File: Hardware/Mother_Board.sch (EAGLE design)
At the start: 11 parts, among them IC1 MAX3232CPE, U1 PIC18F26K22-I/SP

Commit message: Added LCD display module and SPI EEPROM to the schematics.
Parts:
- added JP3: (no value), pinhead:PINHD-1X8
- added JP4, JP5: (no value), pinhead:PINHD-1X6
- added R3: 22R 0.5W, resistor:R-EU_0207/10
- added R4: 10K, rcl:POTENTIOMETER_PT-10S
- added U2: 25LC1024-E/SM, 25LC1024:25LC1024-E/SM
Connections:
- new net N$11: JP3.8, U1.RA0
- new net N$12: JP3.7, U1.RA1
- new net N$15: JP3.6, U1.RA2
- new net N$16: JP3.5, U1.RA3
- new net N$17: JP3.4, U1.RA4
- new net N$18: JP3.3, U1.RA5
- new net N$19: JP3.2, U1.RA6
- new net N$20: JP3.1, U1.RA7
- new net N$21: U1.RC4, U2.SI
- new net N$22: U1.RC3, U2.SCK
- new net N$23: U1.RC5, U2.SO
- new net N$24: U1.RC2, U2.CS*
- new net N$25: JP5.3, R4.1
- new net N$26: JP4.1, U1.RB5
- new net N$27: JP4.2, U1.RB4
- new net N$28: JP4.3, U1.RB3
- new net N$29: JP4.4, U1.RB2
- new net N$30: JP4.5, U1.RB1
- new net N$31: JP4.6, U1.RB0
- new net N$32: JP5.2, R4.3
- new net N$33: JP5.6, R3.2
- net GND: now also JP5.4, JP5.5, U2.VSS
- net VCC: now also JP5.1, R3.1, R4.2, U2.HOLD*, U2.VCC, U2.WP*
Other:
- note added: "/CS1"
- note added: "/CS2"
- note added: "A"
- note added: "D/I"
- note added: "DB0"
- note added: "DB1"
- note added: "DB2"
- note added: "DB3"
- note added: "DB4"
- note added: "DB5"
- note added: "DB6"
- note added: "DB7"
- note added: "Display control"
- note added: "Display data"
- note added: "Display power"
- note added: "E"
- note added: "K"
- note added: "Keyboard"
- note added: "R/W"
- note added: "RST"
- note added: "UART"
- note added: "Vcc"
- note added: "Vee"
- note added: "Vo"
- note added: "Vss"
- note removed: "To DIN keyboard connector"
- note removed: "To Sub-D 9 connector"
- moved on the sheet: C1, C2, C3, C4, C5, IC1, IC1P, JP1

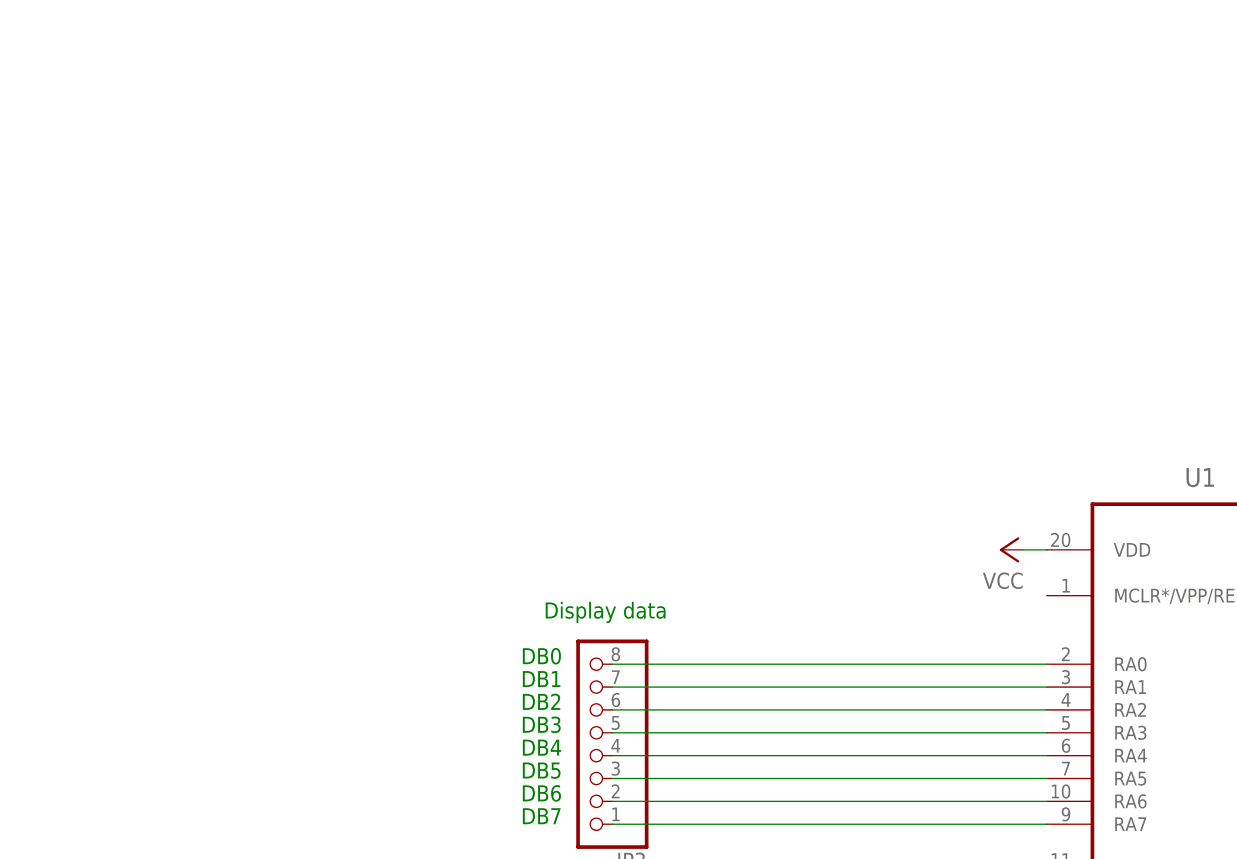
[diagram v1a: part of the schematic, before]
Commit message: Added led and power supply to the schematics.
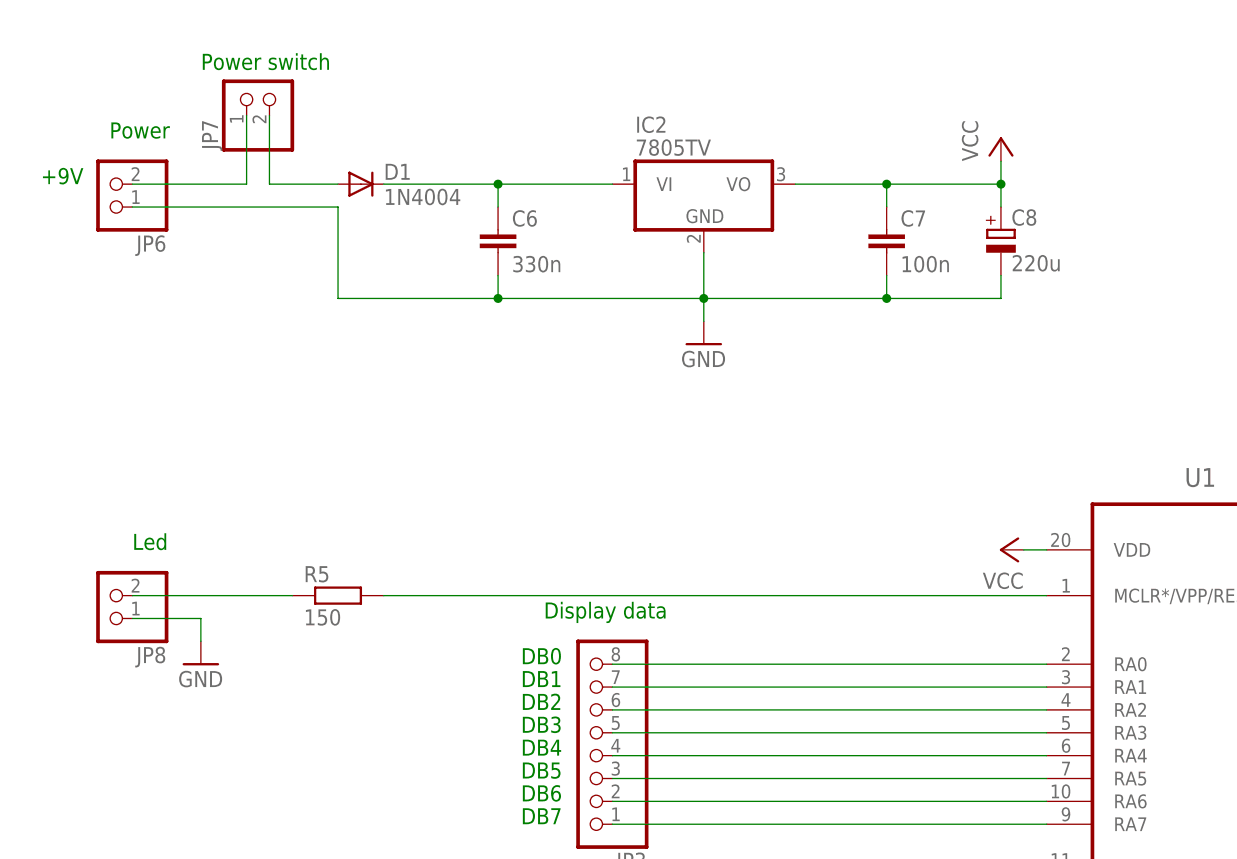
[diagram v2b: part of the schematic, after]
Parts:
- added C6: 330n, rcl:C-EU025-050X050
- added C7: 100n, rcl:C-EU025-030X050
- added C8: 220u, rcl:CPOL-EUB45181A
- added D1: 1N4004, diode:1N4004
- added IC2: 7805TV, linear:7805TV
- added JP6, JP7, JP8: (no value), pinhead:PINHD-1X2
- added R5: 150, rcl:R-EU_0207/10
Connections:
- new net N$34: JP6.2, JP7.1
- new net N$35: D1.A, JP7.2
- new net N$36: C6.1, D1.C, IC2.VI
- new net N$37: R5.2, U1.MCLR*/VPP/RE3
- new net N$38: JP8.2, R5.1
- net GND: now also C6.2, C7.2, C8.-, IC2.GND, JP6.1, JP8.1
- net VCC: now also C7.1, C8.+, IC2.VO
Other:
- note added: "+9V"
- note added: "Led"
- note added: "Power"
- note added: "Power switch"
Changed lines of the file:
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@@
 <part name="R3" library="resistor" deviceset="R-EU_" device="0207/10" value="22R 0.5W"/>
 <part name="P+7" library="supply1" deviceset="VCC" device=""/>
+<part name="IC2" library="linear" deviceset="78*" device="TV" technology="05"/>
+<part name="C6" library="rcl" deviceset="C-EU" device="025-050X050" value="330n"/>
+<part name="D1" library="diode" deviceset="1N4004" device=""/>
+<part name="C8" library="rcl" deviceset="CPOL-EU" device="B45181A" value="220u"/>
+<part name="JP6" library="pinhead" deviceset="PINHD-1X2" device=""/>
+<part name="GND8" library="supply1" deviceset="GND" device=""/>
+<part name="P+9" library="supply1" deviceset="VCC" device=""/>
+<part name="JP7" library="pinhead" deviceset="PINHD-1X2" device=""/>
+<part name="JP8" library="pinhead" deviceset="PINHD-1X2" device=""/>
+<part name="R5" library="rcl" deviceset="R-EU_" device="0207/10" value="150"/>
+<part name="GND10" library="supply1" deviceset="GND" device=""/>
+<part name="C7" library="rcl" deviceset="C-EU" device="025-030X050" value="100n"/>
 </parts>
 <sheets>
@@
 <text x="142.24" y="30.48" size="1.778" layer="91">R/W</text>
 <text x="142.24" y="27.94" size="1.778" layer="91">RST</text>
+<text x="-73.66" y="114.3" size="1.778" layer="91">+9V</text>
+<text x="-66.04" y="119.38" size="1.778" layer="91">Power</text>
+<text x="-55.88" y="127" size="1.778" layer="91">Power switch</text>
+<text x="-63.5" y="73.66" size="1.778" layer="91">Led</text>
 </plain>
 <instances>
@@
 <instance part="R3" gate="G$1" x="129.54" y="-20.32" rot="R90"/>
 <instance part="P+7" gate="VCC" x="129.54" y="-30.48" rot="R180"/>
+<instance part="IC2" gate="A1" x="0" y="114.3"/>
+<instance part="C6" gate="G$1" x="-22.86" y="109.22"/>
+<instance part="D1" gate="1" x="-38.1" y="114.3"/>
+<instance part="C8" gate="G$1" x="33.02" y="109.22"/>
+<instance part="JP6" gate="G$1" x="-66.04" y="114.3" rot="R180"/>
+<instance part="GND8" gate="1" x="0" y="96.52"/>
+<instance part="P+9" gate="VCC" x="33.02" y="119.38"/>
+<instance part="JP7" gate="G$1" x="-48.26" y="124.46" rot="R90"/>
+<instance part="JP8" gate="G$1" x="-66.04" y="68.58" rot="R180"/>
+<instance part="R5" gate="G$1" x="-40.64" y="68.58"/>
+<instance part="GND10" gate="1" x="-55.88" y="60.96"/>
+<instance part="C7" gate="G$1" x="20.32" y="109.22"/>
 </instances>
 <busses>
@@
 <wire x1="129.54" y1="-5.08" x2="116.84" y2="-5.08" width="0.1524" layer="91"/>
 <junction x="129.54" y="-5.08"/>
+</segment>
+<segment>
+<pinref part="JP6" gate="G$1" pin="1"/>
+<wire x1="-63.5" y1="111.76" x2="-40.64" y2="111.76" width="0.1524" layer="91"/>
+<wire x1="-40.64" y1="111.76" x2="-40.64" y2="101.6" width="0.1524" layer="91"/>
+<wire x1="-40.64" y1="101.6" x2="-22.86" y2="101.6" width="0.1524" layer="91"/>
+<pinref part="C6" gate="G$1" pin="2"/>
+<wire x1="0" y1="101.6" x2="20.32" y2="101.6" width="0.1524" layer="91"/>
+<wire x1="20.32" y1="101.6" x2="33.02" y2="101.6" width="0.1524" layer="91"/>
+<wire x1="-22.86" y1="104.14" x2="-22.86" y2="101.6" width="0.1524" layer="91"/>
+<pinref part="GND8" gate="1" pin="GND"/>
+<wire x1="-22.86" y1="101.6" x2="0" y2="101.6" width="0.1524" layer="91"/>
+<wire x1="0" y1="99.06" x2="0" y2="101.6" width="0.1524" layer="91"/>
+<pinref part="IC2" gate="A1" pin="GND"/>
+<wire x1="0" y1="101.6" x2="0" y2="106.68" width="0.1524" layer="91"/>
+<wire x1="20.32" y1="101.6" x2="20.32" y2="104.14" width="0.1524" layer="91"/>
+<pinref part="C8" gate="G$1" pin="-"/>
+<wire x1="33.02" y1="101.6" x2="33.02" y2="104.14" width="0.1524" layer="91"/>
+<junction x="-22.86" y="101.6"/>
+<junction x="0" y="101.6"/>
+<junction x="20.32" y="101.6"/>
+<pinref part="C7" gate="G$1" pin="2"/>
+</segment>
+<segment>
+<pinref part="JP8" gate="G$1" pin="1"/>
+<wire x1="-63.5" y1="66.04" x2="-55.88" y2="66.04" width="0.1524" layer="91"/>
+<pinref part="GND10" gate="1" pin="GND"/>
+<wire x1="-55.88" y1="66.04" x2="-55.88" y2="63.5" width="0.1524" layer="91"/>
 </segment>
 </net>
@@
 <wire x1="129.54" y1="-25.4" x2="129.54" y2="-27.94" width="0.1524" layer="91"/>
 </segment>
+<segment>
+<pinref part="IC2" gate="A1" pin="VO"/>
+<wire x1="10.16" y1="114.3" x2="20.32" y2="114.3" width="0.1524" layer="91"/>
+<wire x1="20.32" y1="111.76" x2="20.32" y2="114.3" width="0.1524" layer="91"/>
+<wire x1="20.32" y1="114.3" x2="33.02" y2="114.3" width="0.1524" layer="91"/>
+<pinref part="C8" gate="G$1" pin="+"/>
+<wire x1="33.02" y1="114.3" x2="33.02" y2="111.76" width="0.1524" layer="91"/>
+<junction x="20.32" y="114.3"/>
+<pinref part="P+9" gate="VCC" pin="VCC"/>
+<wire x1="33.02" y1="116.84" x2="33.02" y2="114.3" width="0.1524" layer="91"/>
+<junction x="33.02" y="114.3"/>
+<pinref part="C7" gate="G$1" pin="1"/>
+</segment>
 </net>
 <net name="N$6" class="0">
@@
 </segment>
 </net>
+<net name="N$36" class="0">
+<segment>
+<pinref part="D1" gate="1" pin="C"/>
+<pinref part="IC2" gate="A1" pin="VI"/>
+<wire x1="-35.56" y1="114.3" x2="-22.86" y2="114.3" width="0.1524" layer="91"/>
+<pinref part="C6" gate="G$1" pin="1"/>
+<wire x1="-22.86" y1="114.3" x2="-10.16" y2="114.3" width="0.1524" layer="91"/>
+<wire x1="-22.86" y1="114.3" x2="-22.86" y2="111.76" width="0.1524" layer="91"/>
+<junction x="-22.86" y="114.3"/>
+</segment>
+</net>
+<net name="N$34" class="0">
+<segment>
+<pinref part="JP6" gate="G$1" pin="2"/>
+<wire x1="-63.5" y1="114.3" x2="-50.8" y2="114.3" width="0.1524" layer="91"/>
+<pinref part="JP7" gate="G$1" pin="1"/>
+<wire x1="-50.8" y1="114.3" x2="-50.8" y2="121.92" width="0.1524" layer="91"/>
+</segment>
+</net>
+<net name="N$35" class="0">
+<segment>
+<pinref part="JP7" gate="G$1" pin="2"/>
+<wire x1="-48.26" y1="121.92" x2="-48.26" y2="114.3" width="0.1524" layer="91"/>
+<pinref part="D1" gate="1" pin="A"/>
+<wire x1="-48.26" y1="114.3" x2="-40.64" y2="114.3" width="0.1524" layer="91"/>
+</segment>
+</net>
+<net name="N$37" class="0">
+<segment>
+<pinref part="U1" gate="A" pin="MCLR*/VPP/RE3"/>
+<wire x1="38.1" y1="68.58" x2="-35.56" y2="68.58" width="0.1524" layer="91"/>
+<pinref part="R5" gate="G$1" pin="2"/>
+</segment>
+</net>
+<net name="N$38" class="0">
+<segment>
+<pinref part="JP8" gate="G$1" pin="2"/>
+<pinref part="R5" gate="G$1" pin="1"/>
+<wire x1="-63.5" y1="68.58" x2="-45.72" y2="68.58" width="0.1524" layer="91"/>
+</segment>
+</net>

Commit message: Added routed PCB.
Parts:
- JP1: value (none) -> UART
- JP2: value (none) -> Keyboard
- JP3: value (none) -> Display data
- JP4: value (none) -> Display control
- JP5: value (none) -> Display power
- JP6: value (none) -> Power
- JP7: value (none) -> Power switch
- JP8: value (none) -> Led
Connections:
- net N$19: now also U1.RA7; no longer U1.RA6
- net N$20: now also U1.RA6; no longer U1.RA7
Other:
- note added: "Routing optimization"
- note removed: "Display control"
- note removed: "Display data"
- note removed: "Display power"
- note removed: "Keyboard"
- note removed: "Led"
- note removed: "Power"
- note removed: "Power switch"
- note removed: "UART"
- moved on the sheet: C5, IC1P
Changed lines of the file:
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@@
 <part name="GND3" library="supply1" deviceset="GND" device=""/>
 <part name="P+1" library="supply1" deviceset="VCC" device=""/>
-<part name="JP1" library="pinhead" deviceset="PINHD-1X3" device=""/>
+<part name="JP1" library="pinhead" deviceset="PINHD-1X3" device="" value="UART"/>
 <part name="GND4" library="supply1" deviceset="GND" device=""/>
-<part name="JP2" library="pinhead" deviceset="PINHD-1X4" device=""/>
+<part name="JP2" library="pinhead" deviceset="PINHD-1X4" device="" value="Keyboard"/>
 <part name="P+2" library="supply1" deviceset="VCC" device=""/>
 <part name="GND5" library="supply1" deviceset="GND" device=""/>
@@
 <part name="R2" library="rcl" deviceset="R-EU_" device="0207/10" value="1K"/>
 <part name="P+4" library="supply1" deviceset="VCC" device=""/>
-<part name="JP3" library="pinhead" deviceset="PINHD-1X8" device=""/>
+<part name="JP3" library="pinhead" deviceset="PINHD-1X8" device="" value="Display data"/>
 <part name="U2" library="25LC1024" deviceset="25LC1024-E/SM" device=""/>
 <part name="GND7" library="supply1" deviceset="GND" device=""/>
 <part name="P+5" library="supply1" deviceset="VCC" device=""/>
 <part name="P+6" library="supply1" deviceset="VCC" device=""/>
-<part name="JP4" library="pinhead" deviceset="PINHD-1X6" device=""/>
-<part name="JP5" library="pinhead" deviceset="PINHD-1X6" device=""/>
+<part name="JP4" library="pinhead" deviceset="PINHD-1X6" device="" value="Display control"/>
+<part name="JP5" library="pinhead" deviceset="PINHD-1X6" device="" value="Display power"/>
 <part name="R4" library="rcl" deviceset="POTENTIOMETER_" device="PT-10S" value="10K"/>
 <part name="P+8" library="supply1" deviceset="VCC" device=""/>
@@
 <part name="D1" library="diode" deviceset="1N4004" device=""/>
 <part name="C8" library="rcl" deviceset="CPOL-EU" device="B45181A" value="220u"/>
-<part name="JP6" library="pinhead" deviceset="PINHD-1X2" device=""/>
+<part name="JP6" library="pinhead" deviceset="PINHD-1X2" device="" value="Power"/>
 <part name="GND8" library="supply1" deviceset="GND" device=""/>
 <part name="P+9" library="supply1" deviceset="VCC" device=""/>
-<part name="JP7" library="pinhead" deviceset="PINHD-1X2" device=""/>
-<part name="JP8" library="pinhead" deviceset="PINHD-1X2" device=""/>
+<part name="JP7" library="pinhead" deviceset="PINHD-1X2" device="" value="Power switch"/>
+<part name="JP8" library="pinhead" deviceset="PINHD-1X2" device="" value="Led"/>
 <part name="R5" library="rcl" deviceset="R-EU_" device="0207/10" value="150"/>
 <part name="GND10" library="supply1" deviceset="GND" device=""/>
@@
 <sheet>
 <plain>
-<text x="172.72" y="63.5" size="1.778" layer="91">UART</text>
-<text x="17.78" y="-25.4" size="1.778" layer="91">Keyboard</text>
-<text x="-17.78" y="66.04" size="1.778" layer="91">Display data</text>
 <text x="-20.32" y="60.96" size="1.778" layer="91">DB0</text>
 <text x="-20.32" y="58.42" size="1.778" layer="91">DB1</text>
@@
 <text x="-20.32" y="50.8" size="1.778" layer="91">DB4</text>
 <text x="-20.32" y="48.26" size="1.778" layer="91">DB5</text>
-<text x="-20.32" y="45.72" size="1.778" layer="91">DB6</text>
-<text x="-20.32" y="43.18" size="1.778" layer="91">DB7</text>
-<text x="129.54" y="48.26" size="1.778" layer="91">Display control</text>
+<text x="-20.32" y="43.18" size="1.778" layer="91">DB6</text>
+<text x="-20.32" y="45.72" size="1.778" layer="91">DB7</text>
 <text x="142.24" y="5.08" size="1.778" layer="91">Vcc</text>
 <text x="142.24" y="2.54" size="1.778" layer="91">Vo</text>
@@
 <text x="142.24" y="-5.08" size="1.778" layer="91">K</text>
 <text x="142.24" y="-7.62" size="1.778" layer="91">A</text>
-<text x="129.54" y="12.7" size="1.778" layer="91">Display power</text>
 <text x="142.24" y="40.64" size="1.778" layer="91">/CS1</text>
 <text x="142.24" y="38.1" size="1.778" layer="91">/CS2</text>
@@
 <text x="142.24" y="27.94" size="1.778" layer="91">RST</text>
 <text x="-73.66" y="114.3" size="1.778" layer="91">+9V</text>
-<text x="-66.04" y="119.38" size="1.778" layer="91">Power</text>
-<text x="-55.88" y="127" size="1.778" layer="91">Power switch</text>
-<text x="-63.5" y="73.66" size="1.778" layer="91">Led</text>
+<text x="5.08" y="38.1" size="1.778" layer="91">Routing optimization</text>
 </plain>
 <instances>
@@
 <instance part="GND1" gate="1" x="167.64" y="83.82"/>
 <instance part="GND2" gate="1" x="167.64" y="96.52"/>
-<instance part="IC1" gate="P" x="139.7" y="116.84"/>
-<instance part="C5" gate="G$1" x="127" y="119.38"/>
-<instance part="GND3" gate="1" x="139.7" y="104.14"/>
-<instance part="P+1" gate="VCC" x="139.7" y="129.54"/>
+<instance part="IC1" gate="P" x="139.7" y="127"/>
+<instance part="C5" gate="G$1" x="127" y="129.54"/>
+<instance part="GND3" gate="1" x="139.7" y="111.76"/>
+<instance part="P+1" gate="VCC" x="139.7" y="142.24"/>
 <instance part="JP1" gate="A" x="177.8" y="71.12"/>
 <instance part="GND4" gate="1" x="170.18" y="60.96"/>
@@
 <pinref part="IC1" gate="P" pin="GND"/>
 <pinref part="GND3" gate="1" pin="GND"/>
-<wire x1="139.7" y1="106.68" x2="139.7" y2="109.22" width="0.1524" layer="91"/>
-<wire x1="139.7" y1="109.22" x2="127" y2="109.22" width="0.1524" layer="91"/>
+<wire x1="139.7" y1="114.3" x2="139.7" y2="116.84" width="0.1524" layer="91"/>
 <pinref part="C5" gate="G$1" pin="2"/>
-<wire x1="127" y1="109.22" x2="127" y2="114.3" width="0.1524" layer="91"/>
+<wire x1="139.7" y1="116.84" x2="139.7" y2="119.38" width="0.1524" layer="91"/>
+<wire x1="127" y1="116.84" x2="127" y2="124.46" width="0.1524" layer="91"/>
+<wire x1="127" y1="116.84" x2="139.7" y2="116.84" width="0.1524" layer="91"/>
+<junction x="139.7" y="116.84"/>
 </segment>
 <segment>
@@
 <segment>
 <pinref part="JP6" gate="G$1" pin="1"/>
-<wire x1="-63.5" y1="111.76" x2="-40.64" y2="111.76" width="0.1524" layer="91"/>
-<wire x1="-40.64" y1="111.76" x2="-40.64" y2="101.6" width="0.1524" layer="91"/>
-<wire x1="-40.64" y1="101.6" x2="-22.86" y2="101.6" width="0.1524" layer="91"/>
+<wire x1="-63.5" y1="111.76" x2="-43.18" y2="111.76" width="0.1524" layer="91"/>
+<wire x1="-43.18" y1="111.76" x2="-43.18" y2="101.6" width="0.1524" layer="91"/>
+<wire x1="-43.18" y1="101.6" x2="-22.86" y2="101.6" width="0.1524" layer="91"/>
 <pinref part="C6" gate="G$1" pin="2"/>
 <wire x1="0" y1="101.6" x2="20.32" y2="101.6" width="0.1524" layer="91"/>
@@
 <net name="VCC" class="0">
 <segment>
-<pinref part="IC1" gate="P" pin="VCC"/>
-<pinref part="P+1" gate="VCC" pin="VCC"/>
-<wire x1="139.7" y1="127" x2="139.7" y2="124.46" width="0.1524" layer="91"/>
-<pinref part="C5" gate="G$1" pin="1"/>
-<wire x1="127" y1="121.92" x2="127" y2="124.46" width="0.1524" layer="91"/>
-<wire x1="127" y1="124.46" x2="139.7" y2="124.46" width="0.1524" layer="91"/>
-</segment>
-<segment>
 <pinref part="U1" gate="A" pin="VDD"/>
 <pinref part="P+2" gate="VCC" pin="VCC"/>
@@
 <pinref part="C7" gate="G$1" pin="1"/>
 </segment>
+<segment>
+<pinref part="C5" gate="G$1" pin="1"/>
+<wire x1="127" y1="132.08" x2="127" y2="137.16" width="0.1524" layer="91"/>
+<wire x1="127" y1="137.16" x2="139.7" y2="137.16" width="0.1524" layer="91"/>
+<pinref part="P+1" gate="VCC" pin="VCC"/>
+<wire x1="139.7" y1="139.7" x2="139.7" y2="137.16" width="0.1524" layer="91"/>
+<pinref part="IC1" gate="P" pin="VCC"/>
+<wire x1="139.7" y1="137.16" x2="139.7" y2="134.62" width="0.1524" layer="91"/>
+<junction x="139.7" y="137.16"/>
+</segment>
 </net>
 <net name="N$6" class="0">
@@
 </segment>
 </net>
-<net name="N$19" class="0">
-<segment>
-<pinref part="U1" gate="A" pin="RA6"/>
-<pinref part="JP3" gate="A" pin="2"/>
-<wire x1="38.1" y1="45.72" x2="-10.16" y2="45.72" width="0.1524" layer="91"/>
-</segment>
-</net>
-<net name="N$20" class="0">
-<segment>
-<pinref part="U1" gate="A" pin="RA7"/>
-<pinref part="JP3" gate="A" pin="1"/>
-<wire x1="38.1" y1="43.18" x2="-10.16" y2="43.18" width="0.1524" layer="91"/>
-</segment>
-</net>
 <net name="N$22" class="0">
 <segment>
@@
 <wire x1="124.46" y1="0" x2="124.46" y2="-2.54" width="0.1524" layer="91"/>
 <pinref part="R4" gate="1" pin="1"/>
-<wire x1="116.84" y1="-2.54" x2="121.92" y2="-2.54" width="0.1524" layer="91"/>
 <wire x1="124.46" y1="-2.54" x2="116.84" y2="-2.54" width="0.1524" layer="91"/>
 </segment>
@@
 </segment>
 </net>
+<net name="N$19" class="0">
+<segment>
+<pinref part="U1" gate="A" pin="RA7"/>
+<wire x1="38.1" y1="43.18" x2="-2.54" y2="43.18" width="0.1524" layer="91"/>
+<wire x1="-2.54" y1="43.18" x2="-2.54" y2="45.72" width="0.1524" layer="91"/>
+<pinref part="JP3" gate="A" pin="2"/>
+<wire x1="-2.54" y1="45.72" x2="-10.16" y2="45.72" width="0.1524" layer="91"/>
+</segment>
+</net>
+<net name="N$20" class="0">
+<segment>
+<wire x1="-5.08" y1="40.64" x2="-5.08" y2="43.18" width="0.1524" layer="91"/>
+<pinref part="JP3" gate="A" pin="1"/>
+<wire x1="-5.08" y1="43.18" x2="-10.16" y2="43.18" width="0.1524" layer="91"/>
+<pinref part="U1" gate="A" pin="RA6"/>
+<wire x1="38.1" y1="45.72" x2="35.56" y2="45.72" width="0.1524" layer="91"/>
+<wire x1="35.56" y1="45.72" x2="35.56" y2="40.64" width="0.1524" layer="91"/>
+<wire x1="35.56" y1="40.64" x2="-5.08" y2="40.64" width="0.1524" layer="91"/>
+</segment>
+</net>
 </nets>
 </sheet>
 </sheets>
+<errors>
+</errors>
 </schematic>
 </drawing>
